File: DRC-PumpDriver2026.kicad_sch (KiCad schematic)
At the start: 42 parts, among them J1 STLINK, J10 Vin_PWR, J2 CAN, J3 CAN, J4 PUMP1, J5 PUMP2, J6 PUMP3, J7 PUMP4, J8 PUMP5, J9 PUMP6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

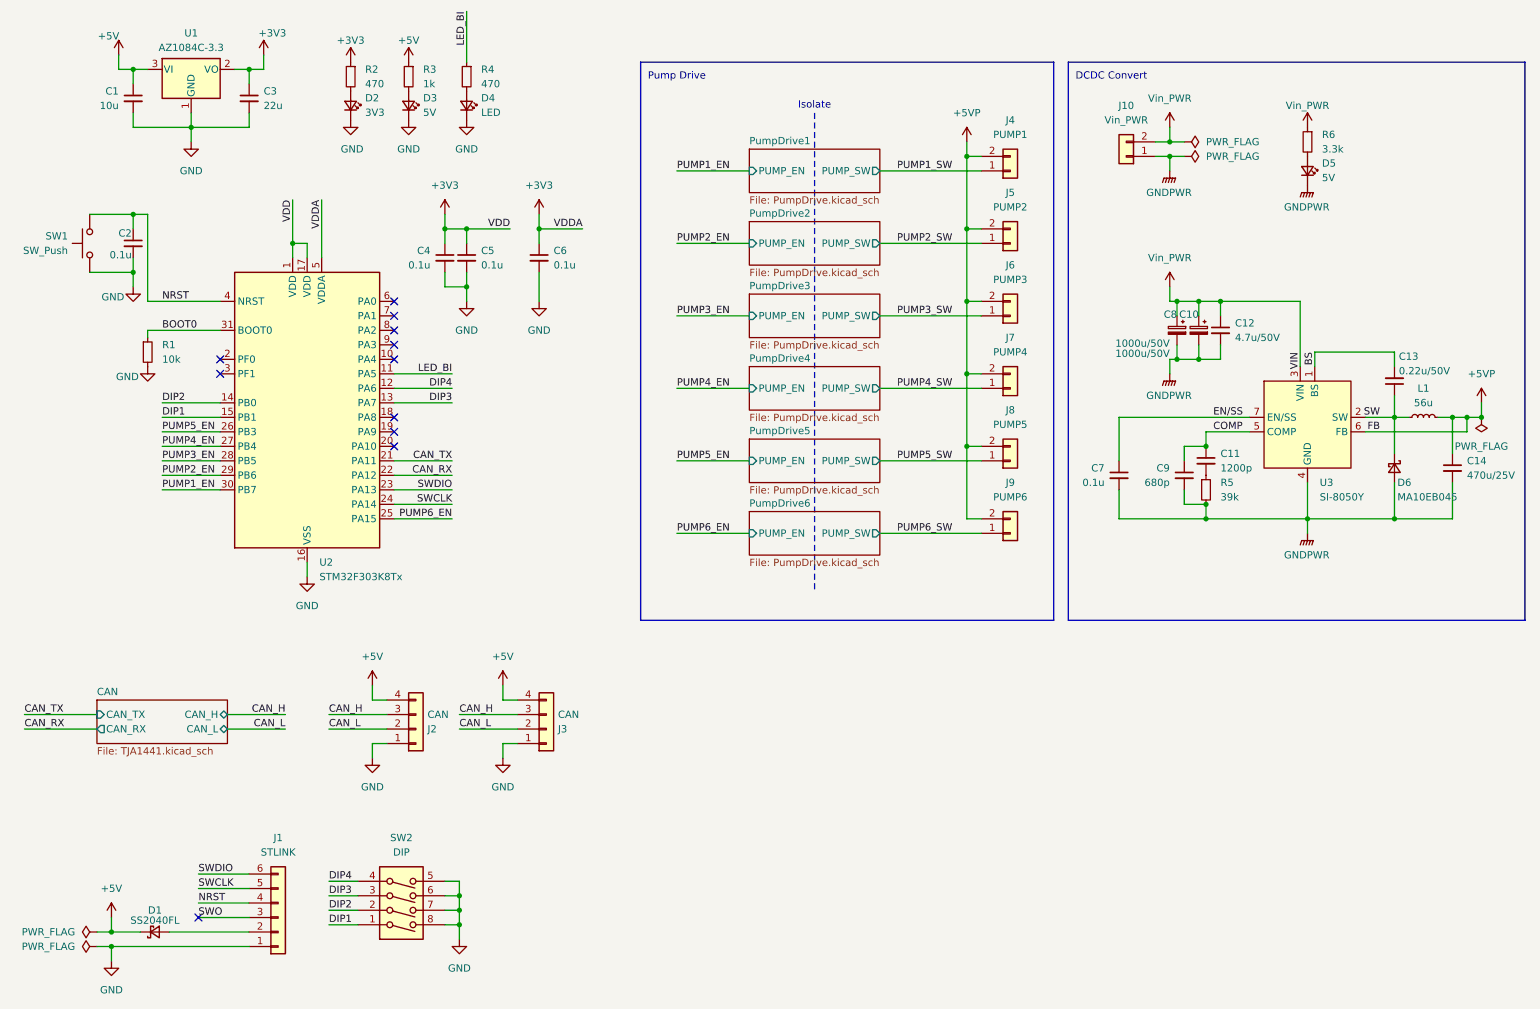
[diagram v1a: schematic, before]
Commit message: DCDCを外して、電源入力に変更、v0.0.2
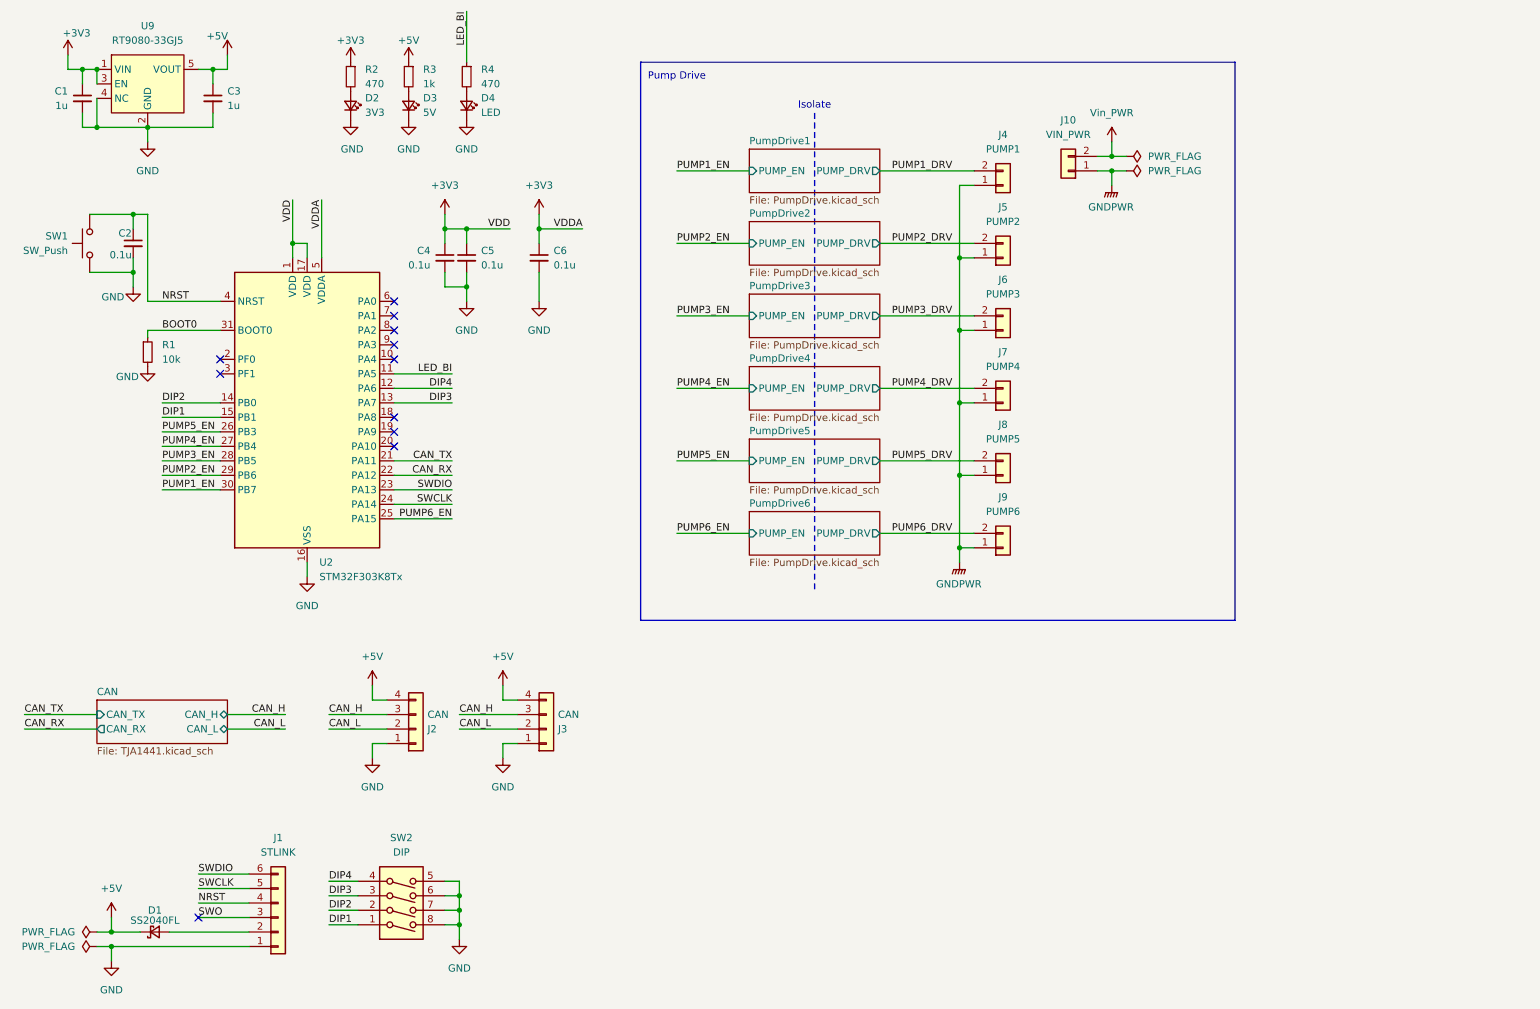
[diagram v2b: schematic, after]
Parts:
- removed C10, C8: 1000u/50V, Capacitor_THT:CP_Radial_D12.5mm_P5.00mm, symbol Device:C_Polarized_Small
- removed C11: 1200p, Capacitor_SMD:C_0603_1608Metric_Pad1.08x0.95mm_HandSolder, symbol Device:C_Small
- removed C12: 4.7u/50V, Capacitor_SMD:C_1206_3216Metric_Pad1.33x1.80mm_HandSolder, symbol Device:C_Small
- removed C13: 0.22u/50V, Capacitor_SMD:C_0603_1608Metric_Pad1.08x0.95mm_HandSolder, symbol Device:C_Small
- removed C14: 470u/25V, Capacitor_THT:CP_Radial_D8.0mm_P3.50mm, symbol Device:C_Small
- removed C7: 0.1u, Capacitor_SMD:C_0603_1608Metric_Pad1.08x0.95mm_HandSolder, symbol Device:C_Small
- removed C9: 680p, Capacitor_SMD:C_0603_1608Metric_Pad1.08x0.95mm_HandSolder, symbol Device:C_Small
- removed D5: 5V, LED_SMD:LED_0603_1608Metric_Pad1.05x0.95mm_HandSolder, symbol Device:LED_Small
- removed D6: MA10EB045, Diode_SMD:Vishay_SMPA, symbol Device:D_Schottky_Small
- removed L1: 56u, Inductor_SMD:L_Bourns_SRP1770TA_16.9x16.9mm, symbol Device:L_Small
- removed R5: 39k, Resistor_SMD:R_0603_1608Metric_Pad0.98x0.95mm_HandSolder, symbol lib:R_Small
- removed R6: 3.3k, Resistor_SMD:R_0603_1608Metric_Pad0.98x0.95mm_HandSolder, symbol lib:R_Small
- removed U1: AZ1084C-3.3, Package_TO_SOT_SMD:TO-252-2, symbol Regulator_Linear:AZ1084-3.3
- removed U3: SI-8050Y, Package_TO_SOT_THT:TO-220F-7_P2.54x3.7mm_StaggerOdd_Lead3.5mm_Vertical, symbol lib:SI-8050Y
- added U9: RT9080-33GJ5, Package_TO_SOT_SMD:TSOT-23-5, symbol lib:RT9080-33GJ5
- C1: value 10u -> 1u
- C3: value 22u -> 1u
- J10: value Vin_PWR -> VIN_PWR
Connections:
- net PUMP1_SW is gone; now on net GNDPWR: J4.1 (Pin_1)
- net PUMP2_SW is gone; now on net GNDPWR: J5.1 (Pin_1)
- net PUMP3_SW is gone; now on net GNDPWR: J6.1 (Pin_1)
- net PUMP4_SW is gone; now on net GNDPWR: J7.1 (Pin_1)
- net PUMP5_SW is gone; now on net GNDPWR: J8.1 (Pin_1)
- net PUMP6_SW is gone; now on net GNDPWR: J9.1 (Pin_1)
- net +3V3: now also C1.1, U9.1 (VIN), U9.3 (EN); no longer C3.1
- net +5V: now also C3.1, U9.5 (VOUT); no longer C1.1
- net GND: now also U9.2 (GND), U9.4 (NC)
- removed net +5VP: J4.2 (Pin_2), J5.2 (Pin_2), J6.2 (Pin_2), J7.2 (Pin_2), J8.2 (Pin_2), J9.2 (Pin_2)
- new net PUMP1_DRV: J4.2 (Pin_2)
- new net PUMP2_DRV: J5.2 (Pin_2)
- new net PUMP3_DRV: J6.2 (Pin_2)
- new net PUMP4_DRV: J7.2 (Pin_2)
- new net PUMP5_DRV: J8.2 (Pin_2)
- new net PUMP6_DRV: J9.2 (Pin_2)
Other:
- sheet PumpDrive1 ports: added PUMP_DRV; removed PUMP_SW
- sheet PumpDrive2 ports: added PUMP_DRV; removed PUMP_SW
- sheet PumpDrive3 ports: added PUMP_DRV; removed PUMP_SW
- sheet PumpDrive4 ports: added PUMP_DRV; removed PUMP_SW
- sheet PumpDrive5 ports: added PUMP_DRV; removed PUMP_SW
- sheet PumpDrive6 ports: added PUMP_DRV; removed PUMP_SW
- note removed: "DCDC Convert"
- moved on the sheet: C1, C3, J10, J4, J5, J6, J7, J8, J9

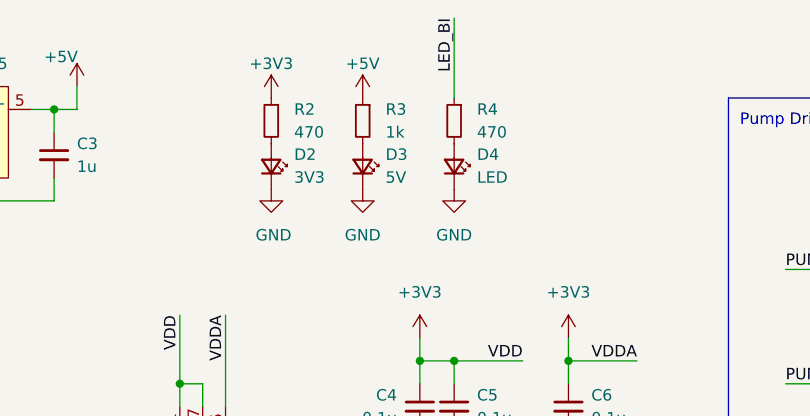
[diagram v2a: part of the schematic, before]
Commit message: CubeMXプロジェクトを追加
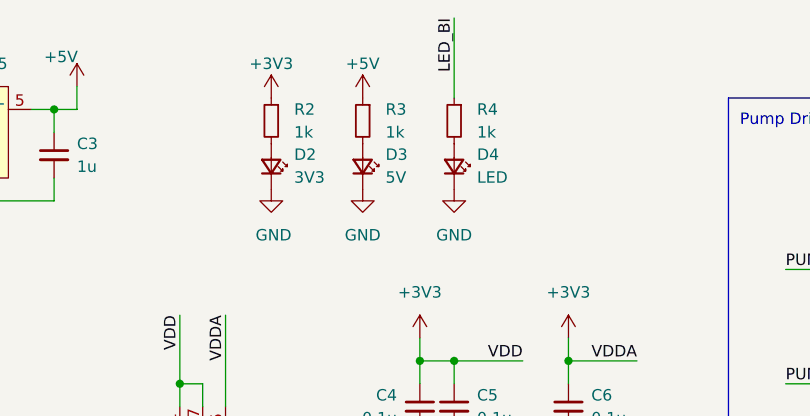
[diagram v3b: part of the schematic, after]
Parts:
- R2, R4: value 470 -> 1k
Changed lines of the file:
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@@
 			)
 		)
-		(property "Value" "470"
+		(property "Value" "1k"
 			(at 80.01 26.6699 0)
 			(effects
@@
 			)
 		)
-		(property "Value" "470"
+		(property "Value" "1k"
 			(at 100.33 26.6699 0)
 			(effects
